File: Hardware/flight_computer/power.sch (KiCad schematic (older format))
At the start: 48 parts

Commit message: added more components, added buzzer, servo circuits, re-arranged some power
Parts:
- removed C?: C_220u, drone_footprints:UWT0G221MCL6GS, symbol openDrone_parts:C_220u
- removed D?: D_Schottky_70V, Diodes_SMD:D_SOD-523, symbol openDrone_parts:D_Schottky_70V
- removed F?: PTC_6V_2A, Fuse_Holders_and_Fuses:Fuse_SMD1206_HandSoldering, symbol openDrone_parts:PTC_6V_2A
- removed F?: PTC_16V_350MA, Resistors_SMD:R_0805_HandSoldering, symbol openDrone_parts:PTC_16V_350MA
- removed F?: PTC_6V_1A, Resistors_SMD:R_0805_HandSoldering, symbol openDrone_parts:PTC_6V_1A
- removed Q?: PMOS_20V_0.4A, TO_SOT_Packages_SMD:SOT-323_SC-70, symbol openDrone_parts:PMOS_20V_0.4A
- removed R?: R_1K, Resistors_SMD:R_0805, symbol openDrone_parts:R_1K
- added F1: PTC_6V_2A, Fuse_Holders_and_Fuses:Fuse_SMD1206_HandSoldering, symbol openDrone_parts:PTC_6V_2A
- added F2, F3: PTC_6V_1A, Resistors_SMD:R_0805_HandSoldering, symbol openDrone_parts:PTC_6V_1A
- added Q3: PMOS_20V_.76A, drone_footprints:NTA4151PT1G, symbol openDrone_parts:PMOS_20V_.76A
- added R17: R_69K8, Resistors_SMD:R_0805, symbol openDrone_parts:R_69K8
- added R18, R21, R22: R_10K, Resistors_SMD:R_0805, symbol openDrone_parts:R_10K
- gave numbers to parts that had none: 41
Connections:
- net labels added: VBAT_SENSE, VDD_3V3_RADIO, VDD_3V3_STM, VDD_5V_AUX, VDD_5V_BUCK, VDD_5V_RADIO, VDD_5V_SENSE, VDD_5V_USB, VDD_BUCK_VALID, VDD_USB_VALID
- net labels removed: FMU_VBAT, FMU_VDD_3V3, VBUS, VBUS_VALID, VDD_3V3_PERIPH, VDD_3V3_SPEKTRUM, VDD_5V, VDD_5V_BRICK, VDD_5V_PERIPH, VDD_5V_RECEIVER, VDD_BRICK_VALID
- wire segments 129 -> 130
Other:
- note added: "BATTERY = VBAT\nBUCK CONVERTER OUTPUT (VDD_5V_BRICK) = VDD_5V_BUCK\nUSB POWER (VBUS) = VDD_5V_USB\nRADIO 5V (VDD_5V_RECEIVER) = VDD_5V_RADIO\nGENERAL 5V (VDD_5V_IN) = VDD_5V_IN\nTELEM/FRSKY (VDD_5V_PERIPH) = VDD_5V_AUX\nSTM POWER (FMU_VDD_3V3) = VDD_3V3_STM\nSENSORS POWER (VDD_3V3_SENSORS) = VDD_3V3_SENSORS\nRADIO POWER (VDD_3V3_SPEKTRUM) = VDD_3V3_RADIO\n"
- note removed: "BATTERY = VBAT\nBUCK CONVERTER OUTPUT (VDD_5V_BRICK) = VDD_5V_BUCK\nUSB POWER (VBUS) = VDD_5V_USB\nRADIO 5V (VDD_5V_RECEIVER) = VDD_5V_RADIO\nGENERAL 5V (VDD_5V_IN) = VDD_5V_IN\nTELEM/FRSKY (VDD_5V_PERIPH) = VDD_5V_TELEM\nSTM POWER (FMU_VDD_3V3) = VDD_3V3_STM\nSENSORS POWER (VDD_3V3_SENSORS) = VDD_3V3_SENSORS\nRADIO POWER (VDD_3V3_SPEKTRUM) = RADIO_VDD_3V3\n"
- moved on the sheet: C28, C31, C33, FL1, R32, U8

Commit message: Finishes v1 connections
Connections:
- net SPEKTRUM_POWER renamed SPEKTRUM_POWER_CTRL
- net VDD_3V3_PERIPH_EN renamed VDD_3V3_RADIO_EN
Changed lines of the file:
@@
 Wire Wire Line
 	12300 5300 12600 5300
-Text HLabel 11650 5400 0    50   Input ~ 0
-VDD_3V3_PERIPH_EN
 Wire Wire Line
 	11650 5400 11850 5400
@@
 	13550 5300 14050 5300
 Text HLabel 14750 4800 2    50   Input ~ 0
-SPEKTRUM_POWER
+SPEKTRUM_POWER_CTRL
 Wire Wire Line
 	14750 4800 14500 4800
@@
 PERIPHERAL POWER LDO 3V3
 Wire Notes Line
-	15700 6400 15700 4400
-Wire Notes Line
-	15700 4400 10750 4400
-Wire Notes Line
 	10750 4400 10750 6400
-Wire Notes Line
-	10750 6400 15700 6400
-Text HLabel 5700 1150 2    50   Input ~ 0
-VDD_5V_BUCK
 Wire Notes Line
 	6350 750  6350 2550
@@
 Text HLabel 2500 6400 2    50   Input ~ 0
 VDD_5V_SENSE
-Text HLabel 1350 4100 0    50   Input ~ 0
-VDD_5V_BUCK
 Text HLabel 14650 3300 2    50   Input ~ 0
 VDD_3V3_SENSORS
@@
 	1    0    0    -1
 $EndComp
+Text Label 5700 1150 0    50   ~ 0
+VDD_5V_BUCK
+Text Label 1350 4100 2    50   ~ 0
+VDD_5V_BUCK
+Wire Notes Line
+	10750 4400 15800 4400
+Wire Notes Line
+	10750 6400 15800 6400
+Wire Notes Line
+	15800 4400 15800 6400
+Text HLabel 11650 5400 0    50   Input ~ 0
+VDD_3V3_RADIO_EN
 $EndSCHEMATC

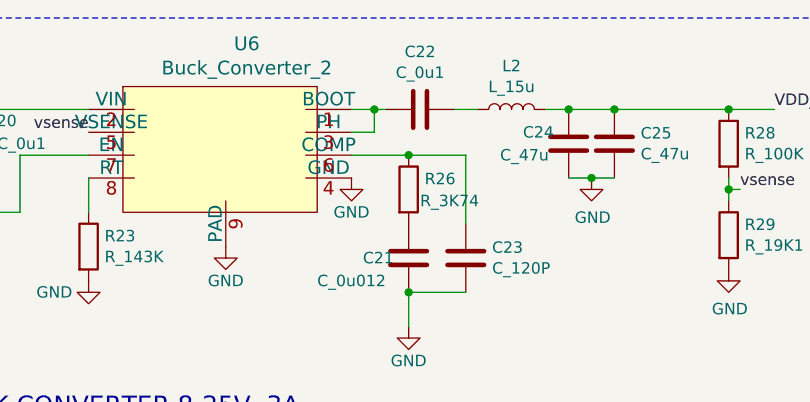
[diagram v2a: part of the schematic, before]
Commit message: fixed buck converter issue
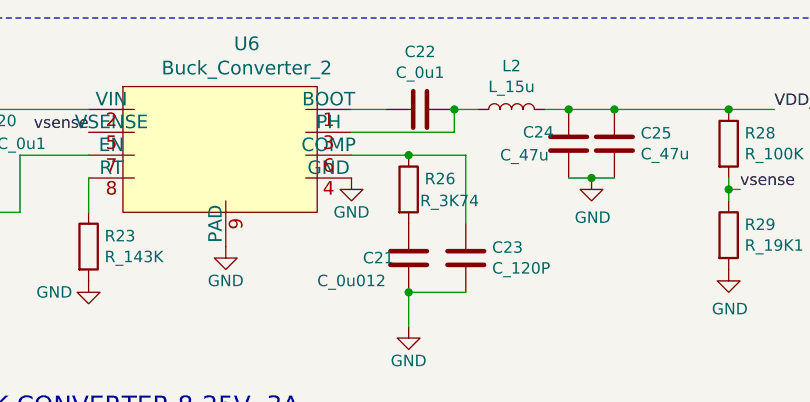
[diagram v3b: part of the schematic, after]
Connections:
- net at C22.2, U6.1 (BOOT): no longer U6.3 (PH)
- net at C22.1, L2.1: now also U6.3 (PH)
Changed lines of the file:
@@
 	4350 1350 4350 1650
 Connection ~ 4100 1350
-Wire Wire Line
-	3850 1150 3950 1150
 $Comp
 L openDrone_parts:C_0u1 C22
@@
 	0    1    1    0
 $EndComp
-Wire Wire Line
-	3850 1250 3950 1250
-Wire Wire Line
-	3950 1250 3950 1150
-Connection ~ 3950 1150
-Wire Wire Line
-	3950 1150 4000 1150
 Wire Wire Line
 	4300 1150 4400 1150
@@
 Text HLabel 11650 5400 0    50   Input ~ 0
 VDD_3V3_RADIO_EN
+Wire Wire Line
+	3850 1150 4000 1150
+Wire Wire Line
+	3850 1250 4300 1250
+Wire Wire Line
+	4300 1250 4300 1150
+Connection ~ 4300 1150
 $EndSCHEMATC

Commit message: worked on layout
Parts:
- removed Q3: PMOS_20V_.76A, drone_footprints:NTA4151PT1G, symbol openDrone_parts:PMOS_20V_.76A
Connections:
- net VDD_3V3_RADIO: now also C30.1, C32.1, U7.5 (VO)
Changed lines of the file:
@@
 Wire Wire Line
 	13550 5300 14050 5300
-Text HLabel 14750 4800 2    50   Input ~ 0
-SPEKTRUM_POWER_CTRL
-Wire Wire Line
-	14750 4800 14500 4800
-Wire Wire Line
-	14500 4800 14500 4850
-Wire Wire Line
-	14300 5150 14050 5150
-Wire Wire Line
-	14050 5150 14050 5300
-Connection ~ 14050 5300
-Text HLabel 14700 5150 2    50   Input ~ 0
+Text HLabel 14150 5300 2    50   Input ~ 0
 VDD_3V3_RADIO
 Text Notes 14850 2650 0    79   ~ 0
@@
 	14500 1250 14900 1250
 $Comp
-L openDrone_parts:PMOS_20V_.76A Q3
-U 1 1 5FAD41DB
-P 14500 5050
-F 0 "Q3" V 14749 5050 50  0000 C CNN
-F 1 "PMOS_20V_.76A" V 14840 5050 50  0000 C CNN
-F 2 "drone_footprints:NTA4151PT1G" H 13950 5350 50  0001 C CNN
-F 3 "" H 14500 5050 50  0001 C CNN
-F 4 "NTA4151PT1GOSCT-ND" H 14000 5250 50  0001 C CNN "DPN"
-F 5 "NTA4151PT1G" H 13850 5150 50  0001 C CNN "MPN"
-	1    14500 5050
-	0    1    1    0
-$EndComp
-$Comp
 L openDrone_parts:PTC_6V_2A F1
 U 1 1 5FB0D3CF
@@
 	4300 1250 4300 1150
 Connection ~ 4300 1150
+Connection ~ 14050 5300
+Wire Wire Line
+	14050 5300 14150 5300
 $EndSCHEMATC

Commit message: updated LEDs
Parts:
- removed D5: LED_GREEN, LEDs:LED_0603_HandSoldering, symbol openDrone_parts:LED_GREEN
- removed R27: R_220, Resistors_SMD:R_0805, symbol openDrone_parts:R_220
- added D5: LED_0805_Green, drone_footprints:LED_0805, symbol openDrone_parts:LED_0805_Green
- added R35: R_120, Resistors_SMD:R_0805, symbol openDrone_parts:R_120
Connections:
- net GND: now also R35.2
- net VDD_5V_IN: now also D5.2 (A)
- new net: D5.1 (K), R35.1
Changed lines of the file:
@@
 	1    0    0    -1
-$EndComp
-$Comp
-L openDrone_parts:R_220 R?
-U 1 1 5F8C121B
-P 4250 4250
-AR Path="/5F615F42/5F8C121B" Ref="R?"  Part="1"
-AR Path="/5F84A65B/5F8C121B" Ref="R27"  Part="1"
-F 0 "R27" V 4204 4320 50  0000 L CNN
-F 1 "R_220" V 4295 4320 50  0000 L CNN
-F 2 "Resistors_SMD:R_0805" H 3450 4400 50  0001 C CNN
-F 3 "" H 3950 4750 50  0001 C CNN
-F 4 "311-220CRCT-ND" H 3600 4500 60  0001 C CNN "DPN"
-	1    4250 4250
-	0    1    1    0
-$EndComp
-$Comp
-L openDrone_parts:LED_GREEN D?
-U 1 1 5F8C1214
-P 4250 3800
-AR Path="/5F615F42/5F8C1214" Ref="D?"  Part="1"
-AR Path="/5F84A65B/5F8C1214" Ref="D5"  Part="1"
-F 0 "D5" V 4211 3918 50  0000 L CNN
-F 1 "LED_GREEN" V 4302 3918 50  0000 L CNN
-F 2 "LEDs:LED_0603_HandSoldering" H 4300 3600 50  0001 C CNN
-F 3 "https://www.digikey.com/product-detail/en/kingbright/APTD1608CGCK/754-1545-1-ND/2514673" H 4250 3800 50  0001 C CNN
-F 4 "754-1545-1-ND" H 4250 3550 50  0001 C CNN "DPN"
-	1    4250 3800
-	0    1    1    0
 $EndComp
 Wire Wire Line
@@
 Wire Wire Line
 	14050 5300 14150 5300
+$Comp
+L openDrone_parts:LED_0805_Green D5
+U 1 1 5F8E98E7
+P 4250 3800
+F 0 "D5" V 4289 3683 50  0000 R CNN
+F 1 "LED_0805_Green" V 4198 3683 50  0000 R CNN
+F 2 "drone_footprints:LED_0805" H 3550 4050 50  0001 C CNN
+F 3 "http://www.osram-os.com/Graphics/XPic9/00078860_0.pdf" H 4250 3900 50  0001 C CNN
+F 4 "475-1410-1-ND" H 3600 4150 60  0001 C CNN "DPN"
+F 5 "LG R971-KN-1" H 3400 3950 60  0001 C CNN "MPN"
+F 6 "https://www.digikey.com/products/en?keywords=475-1410-1-ND" H 4650 4300 60  0001 C CNN "PurchasingLink"
+	1    4250 3800
+	0    -1   -1   0
+$EndComp
+$Comp
+L openDrone_parts:R_120 R35
+U 1 1 5F8EA923
+P 4250 4250
+F 0 "R35" V 4204 4320 50  0000 L CNN
+F 1 "R_120" V 4295 4320 50  0000 L CNN
+F 2 "Resistors_SMD:R_0805" H 3450 4400 50  0001 C CNN
+F 3 "" H 3950 4750 50  0001 C CNN
+F 4 "A129738CT-ND" H 3600 4500 60  0001 C CNN "DPN"
+	1    4250 4250
+	0    1    1    0
+$EndComp
 $EndSCHEMATC

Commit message: added switch components, worked on layout. Sensor 3V3 unfinished.
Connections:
- no-connect marks 0 -> 1
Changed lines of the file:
@@
 	0    1    1    0
 $EndComp
+NoConn ~ 13200 5400
 $EndSCHEMATC
